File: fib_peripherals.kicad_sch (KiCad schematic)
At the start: 2 parts, among them J704 Conn_02x20_Odd_Even, J801 Conn_02x20_Odd_Even

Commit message: started arranging the components on the board, added some more missing footprints. starting to think about the overall distribution of parts
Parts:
- removed J704, J801: Conn_02x20_Odd_Even, Connector_PinHeader_2.54mm:PinHeader_2x20_P2.54mm_Vertical, symbol Connector_Generic:Conn_02x20_Odd_Even
- added J1, J2: Raspi_Header, Fibel2:Raspberry_Bottom_Entry, symbol Fibel2:Raspi_Header
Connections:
- net D3V3: now also J1.1 (Pin_1), J1.17 (Pin_17)
- net GND: now also J1.14 (Pin_14), J1.20 (Pin_20), J1.25 (Pin_25), J1.30 (Pin_30), J1.34 (Pin_34), J1.39 (Pin_39), J1.6 (Pin_6), J1.9 (Pin_9), J2.14 (Pin_14), J2.20 (Pin_20), J2.25 (Pin_25), J2.30 (Pin_30), J2.34 (Pin_34), J2.39 (Pin_39), J2.6 (Pin_6), J2.9 (Pin_9)
- net I2C1_SCL: now also J1.5 (Pin_5)
- net I2C1_SDA: now also J1.3 (Pin_3)
- net I2S0_DIN: now also J1.38 (Pin_38)
- net I2S0_DOUT: now also J1.40 (Pin_40)
- net I2S0_FS: now also J1.35 (Pin_35)
- net I2S0_SCLK: now also J1.12 (Pin_12)
- net IT8951_HRDY0: now also J2.18 (Pin_18)
- net IT8951_RST0: now also J2.11 (Pin_11)
- net IT8951_SPI1_CS0: now also J2.24 (Pin_24)
- net IT8951_SPI1_MISO: now also J2.21 (Pin_21)
- net IT8951_SPI1_MOSI: now also J2.19 (Pin_19)
- net IT8951_SPI1_SCK: now also J2.23 (Pin_23)
- net RP_GPIO04: now also J1.7 (Pin_7)
- net RP_GPIO05: now also J1.29 (Pin_29)
- net RP_GPIO06: now also J1.31 (Pin_31)
- net RP_GPIO12: now also J1.32 (Pin_32)
- net RP_GPIO13: now also J1.33 (Pin_33)
- net RP_GPIO16: now also J1.36 (Pin_36)
- net RP_GPIO17: now also J1.11 (Pin_11)
- net RP_GPIO22: now also J1.15 (Pin_15)
- net RP_GPIO23: now also J1.16 (Pin_16)
- net RP_GPIO24: now also J1.18 (Pin_18)
- net RP_GPIO25: now also J1.22 (Pin_22)
- net RP_GPIO26: now also J1.37 (Pin_37)
- net RP_GPIO27: now also J1.13 (Pin_13)
- net RP_ID_SC: now also J1.28 (Pin_28)
- net RP_ID_SD: now also J1.27 (Pin_27)
- net SPI0_CS0: now also J1.24 (Pin_24)
- net SPI0_CS1: now also J1.26 (Pin_26)
- net SPI0_MISO: now also J1.21 (Pin_21)
- net SPI0_MOSI: now also J1.19 (Pin_19)
- net SPI0_SCK: now also J1.23 (Pin_23)
- net UART1_RXD: now also J1.10 (Pin_10)
- net UART1_TXD: now also J1.8 (Pin_8)
- net VDD_MOD: now also J1.2 (Pin_2), J1.4 (Pin_4), J2.2 (Pin_2), J2.4 (Pin_4)

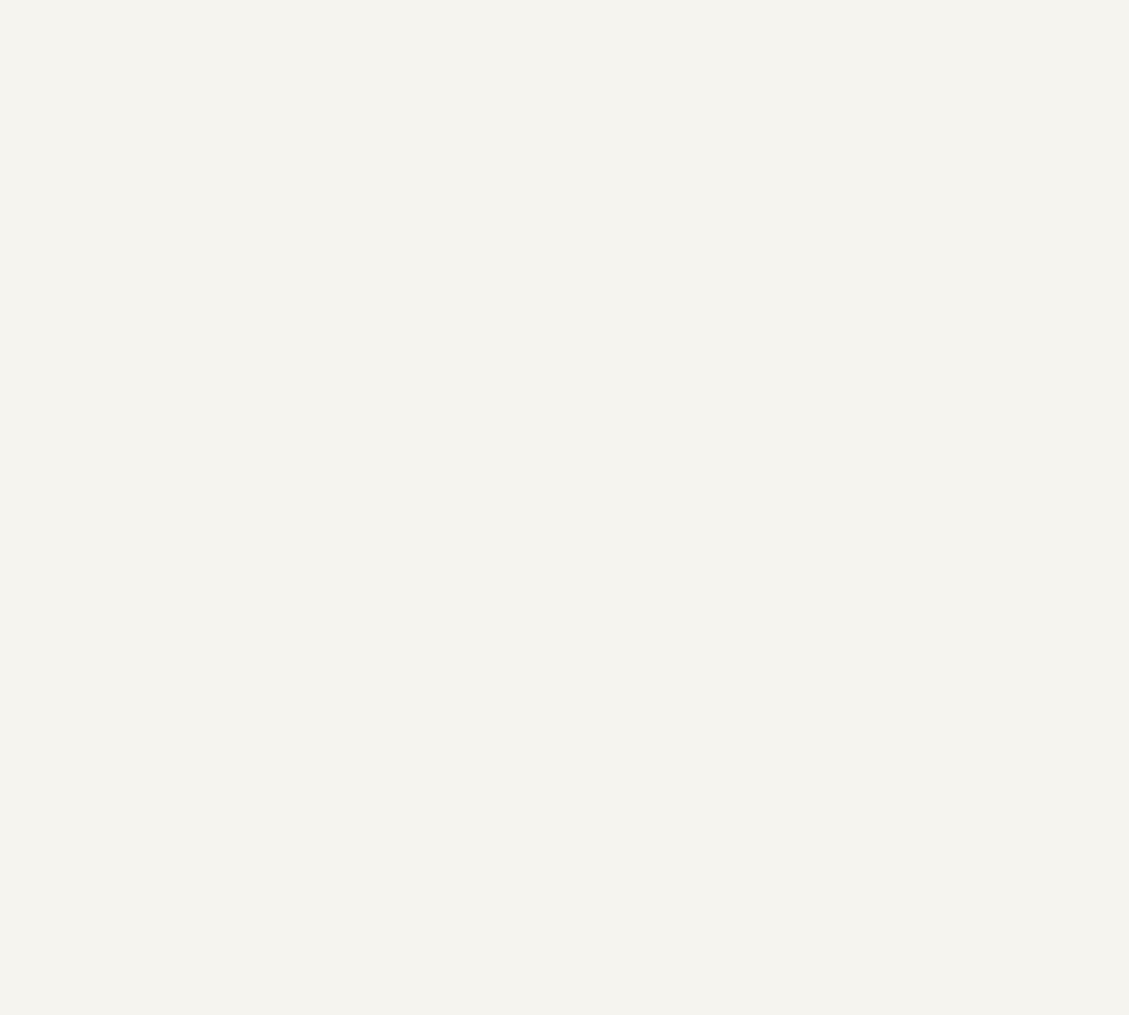
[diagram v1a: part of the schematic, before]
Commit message: replaced 1v8 buck with ldo, added startup circuit, added footprints for eink connectors
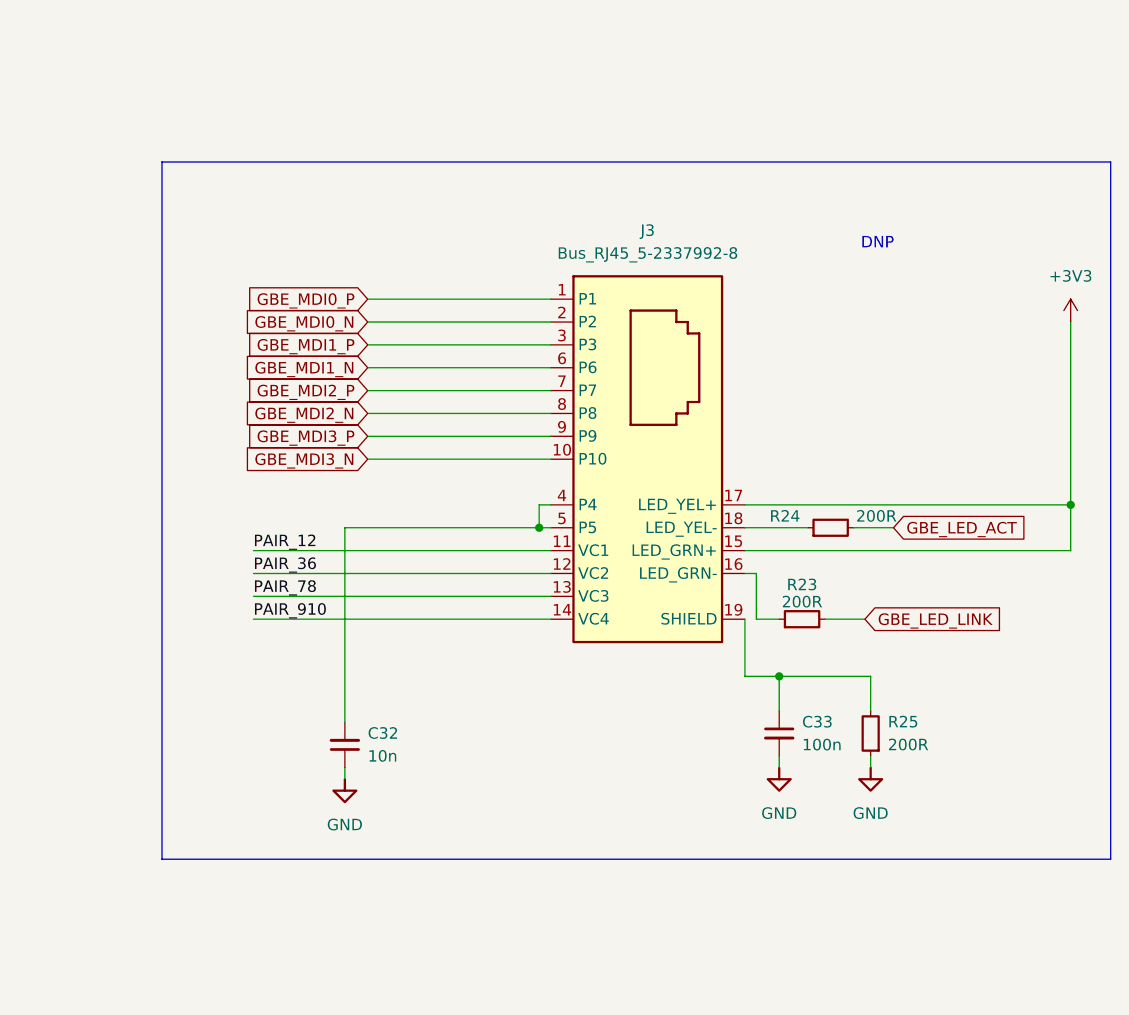
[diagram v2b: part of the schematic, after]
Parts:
- added C32: C_10n_0603, antmicro-footprints:C_0603_1608Metric, symbol antmicroCapacitors0603:C_10n_0603
- added C33: C_100n_0402, antmicro-footprints:C_0402_1005Metric, symbol antmicroCapacitors0402:C_100n_0402
- added J3: Bus_RJ45_5-2337992-8, antmicro-footprints:RJ45_X-2337992-8_Horizontal, symbol antmicroModularConnectorsJacksWithMagnetics:Bus_RJ45_5-2337992-8
- added R23, R24, R25: R_200R_0402, antmicro-footprints:R_0402_1005Metric, symbol antmicroResistors0402:R_200R_0402
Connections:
- net GND: now also C32.1, C33.2, R25.1
- new net: J3.18 (LED_YEL-), R24.1
- new net: C33.1, J3.19 (SHIELD), J3.20 (SHIELD), R25.2
- new net: C32.2, J3.4 (P4), J3.5 (P5)
- new net: J3.16 (LED_GRN-), R23.1
- new net +3V3: J3.15 (LED_GRN+), J3.17 (LED_YEL+)
- new net GBE_LED_ACT: R24.2
- new net GBE_LED_LINK: R23.2
- new net GBE_MDI0_N: J3.2 (P2)
- new net GBE_MDI0_P: J3.1 (P1)
- new net GBE_MDI1_N: J3.6 (P6)
- new net GBE_MDI1_P: J3.3 (P3)
- new net GBE_MDI2_N: J3.8 (P8)
- new net GBE_MDI2_P: J3.7 (P7)
- new net GBE_MDI3_N: J3.10 (P10)
- new net GBE_MDI3_P: J3.9 (P9)
- new net PAIR_12: J3.11 (VC1)
- new net PAIR_36: J3.12 (VC2)
- new net PAIR_78: J3.13 (VC3)
- new net PAIR_910: J3.14 (VC4)
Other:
- note added: "DNP"

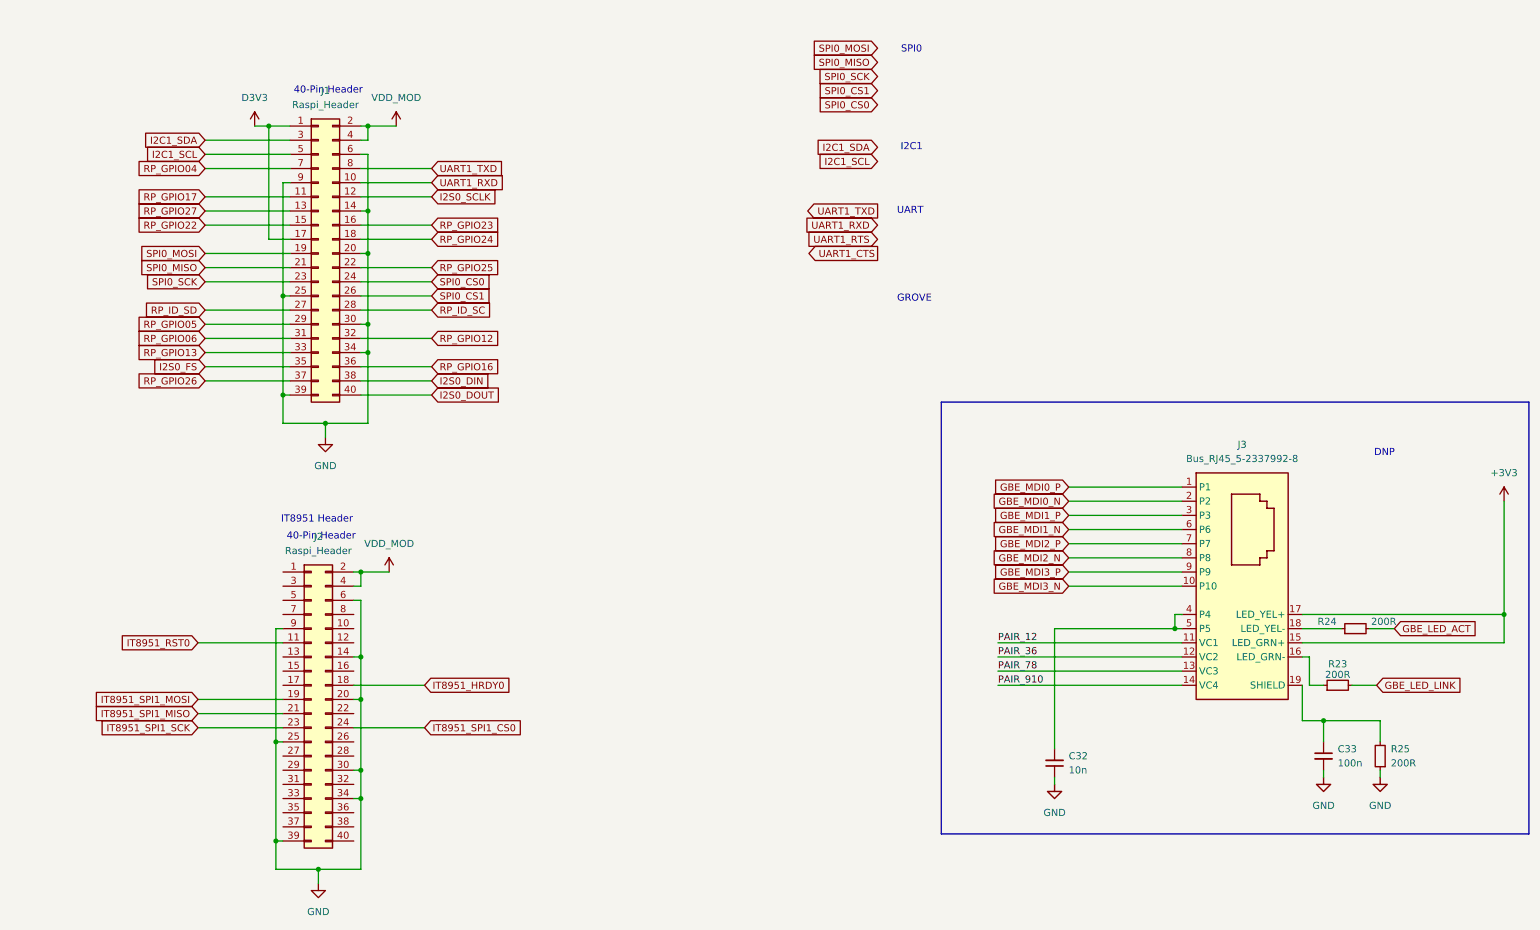
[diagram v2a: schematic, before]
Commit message: added all missing footprints, fixed library & footprint links, did layout out 99% of components, all that's left is rtc(?), peripherals, routing & lengthmatching and final sanity checks
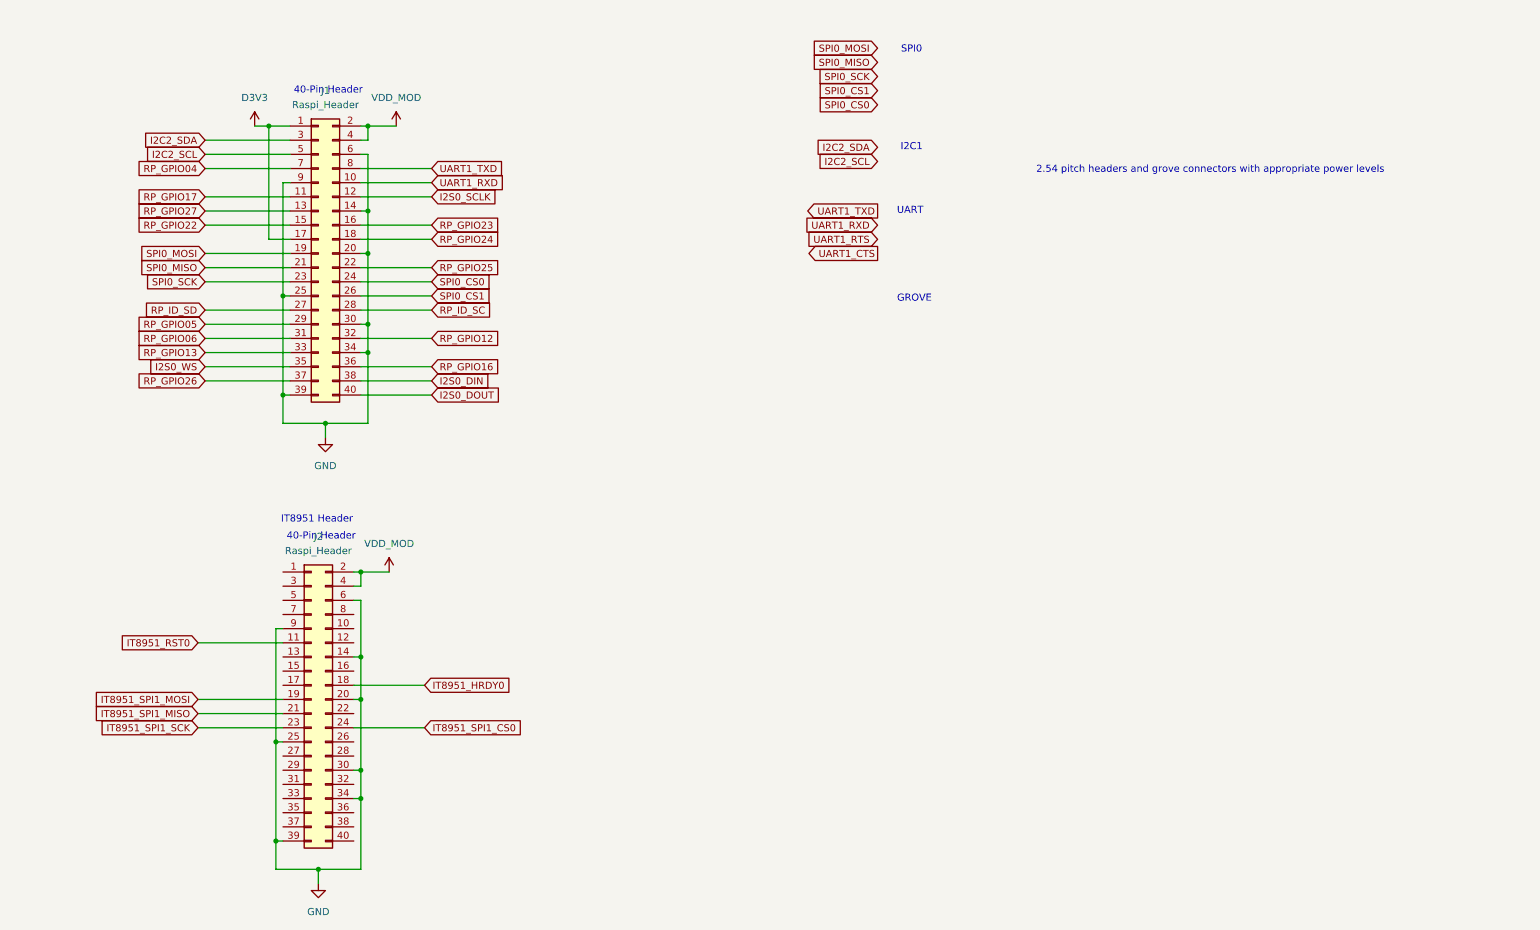
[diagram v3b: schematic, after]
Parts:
- removed C32: C_10n_0603, antmicro-footprints:C_0603_1608Metric, symbol antmicroCapacitors0603:C_10n_0603
- removed C33: C_100n_0402, antmicro-footprints:C_0402_1005Metric, symbol antmicroCapacitors0402:C_100n_0402
- removed J3: Bus_RJ45_5-2337992-8, antmicro-footprints:RJ45_X-2337992-8_Horizontal, symbol antmicroModularConnectorsJacksWithMagnetics:Bus_RJ45_5-2337992-8
- removed R23, R24, R25: R_200R_0402, antmicro-footprints:R_0402_1005Metric, symbol antmicroResistors0402:R_200R_0402
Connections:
- net I2C1_SCL renamed I2C2_SCL
- net I2C1_SDA renamed I2C2_SDA
- net I2S0_FS renamed I2S0_WS
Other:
- note added: "2.54 pitch headers and grove connectors with appropriate power levels"
- note removed: "DNP"

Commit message: did length tuning, routing of final submodules and most of power routing
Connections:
- net D3V3 renamed +3V3
- net VDD_MOD renamed +5V
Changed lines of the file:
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@@
+	)
+	(symbol
+		(lib_id "power:+3V3")
+		(at 54.61 39.37 0)
+		(unit 1)
+		(exclude_from_sim no)
+		(in_bom yes)
+		(on_board yes)
+		(dnp no)
+		(fields_autoplaced yes)
+		(property "Reference" "#PWR083"
+			(at 54.61 43.18 0)
+			(effects
+				(font
+					(size 1.27 1.27)
+				)
+				(hide yes)
+			)
+		)
+		(property "Value" "+3V3"
+			(at 54.61 34.29 0)
+			(effects
+				(font
+					(size 1.27 1.27)
+				)
+			)
+		)
+		(property "Footprint" ""
+			(at 54.61 39.37 0)
+			(effects
+				(font
+					(size 1.27 1.27)
+				)
+				(hide yes)
+			)
+		)
+		(property "Datasheet" ""
+			(at 54.61 39.37 0)
+			(effects
+				(font
+					(size 1.27 1.27)
+				)
+				(hide yes)
+			)
+		)
+		(property "Description" "Power symbol creates a global label with name \"+3V3\""
+			(at 54.61 39.37 0)
+			(effects
+				(font
+					(size 1.27 1.27)
+				)
+				(hide yes)
+			)
+		)
+		(pin "1"
+		)
+		(instances
+			(project "Fibel2"
+				(path "/862c21e2-7ec9-4f80-a33c-aad02ea9423e/a39c2c52-3412-48a6-9504-27933873c1ba"
+					(reference "#PWR083")
+					(unit 1)
+				)
+			)
+		)
 	)
 	(symbol
@@
 	)
 	(symbol
+		(lib_id "power:+5V")
+		(at 80.01 39.37 0)
+		(unit 1)
+		(exclude_from_sim no)
+		(in_bom yes)
+		(on_board yes)
+		(dnp no)
+		(fields_autoplaced yes)
+		(property "Reference" "#PWR082"
+			(at 80.01 43.18 0)
+			(effects
+				(font
+					(size 1.27 1.27)
+				)
+				(hide yes)
+			)
+		)
+		(property "Value" "+5V"
+			(at 80.01 34.29 0)
+			(effects
+				(font
+					(size 1.27 1.27)
+				)
+			)
+		)
+		(property "Footprint" ""
+			(at 80.01 39.37 0)
+			(effects
+				(font
+					(size 1.27 1.27)
+				)
+				(hide yes)
+			)
+		)
+		(property "Datasheet" ""
+			(at 80.01 39.37 0)
+			(effects
+				(font
+					(size 1.27 1.27)
+				)
+				(hide yes)
+			)
+		)
+		(property "Description" "Power symbol creates a global label with name \"+5V\""
+			(at 80.01 39.37 0)
+			(effects
+				(font
+					(size 1.27 1.27)
+				)
+				(hide yes)
+			)
+		)
+		(pin "1"
+		)
+		(instances
+			(project "Fibel2"
+				(path "/862c21e2-7ec9-4f80-a33c-aad02ea9423e/a39c2c52-3412-48a6-9504-27933873c1ba"
+					(reference "#PWR082")
+					(unit 1)
+				)
+			)
+		)
+	)
+	(symbol
 		(lib_id "Fibel2:Raspi_Header")
 		(at 66.04 62.23 0)
@@
 				(path "/862c21e2-7ec9-4f80-a33c-aad02ea9423e/a39c2c52-3412-48a6-9504-27933873c1ba"
 					(reference "J1")
-					(unit 1)
-				)
-			)
-		)
-	)
-	(symbol
-		(lib_id "power:+5V")
-		(at 78.74 119.38 0)
-		(unit 1)
-		(exclude_from_sim no)
-		(in_bom yes)
-		(on_board yes)
-		(dnp no)
-		(fields_autoplaced yes)
-		(property "Reference" "#PWR0713"
-			(at 78.74 123.19 0)
-			(effects
-				(font
-					(size 1.27 1.27)
-				)
-				(hide yes)
-			)
-		)
-		(property "Value" "VDD_MOD"
-			(at 78.74 114.3 0)
-			(effects
-				(font
-					(size 1.27 1.27)
-				)
-			)
-		)
-		(property "Footprint" ""
-			(at 78.74 119.38 0)
-			(effects
-				(font
-					(size 1.27 1.27)
-				)
-				(hide yes)
-			)
-		)
-		(property "Datasheet" ""
-			(at 78.74 119.38 0)
-			(effects
-				(font
-					(size 1.27 1.27)
-				)
-				(hide yes)
-			)
-		)
-		(property "Description" "Power symbol creates a global label with name \"+5V\""
-			(at 78.74 119.38 0)
-			(effects
-				(font
-					(size 1.27 1.27)
-				)
-				(hide yes)
-			)
-		)
-		(pin "1"
-		)
-		(instances
-			(project "Fibel2"
-				(path "/862c21e2-7ec9-4f80-a33c-aad02ea9423e/a39c2c52-3412-48a6-9504-27933873c1ba"
-					(reference "#PWR0713")
 					(unit 1)
 				)
@@
 	)
 	(symbol
-		(lib_id "power:+3V3")
-		(at 54.61 39.37 0)
+		(lib_id "power:+5V")
+		(at 78.74 119.38 0)
 		(unit 1)
 		(exclude_from_sim no)
@@
 		(dnp no)
 		(fields_autoplaced yes)
-		(property "Reference" "#PWR0801"
-			(at 54.61 43.18 0)
-			(effects
-				(font
-					(size 1.27 1.27)
-				)
-				(hide yes)
-			)
-		)
-		(property "Value" "D3V3"
-			(at 54.61 34.29 0)
+		(property "Reference" "#PWR081"
+			(at 78.74 123.19 0)
+			(effects
+				(font
+					(size 1.27 1.27)
+				)
+				(hide yes)
+			)
+		)
+		(property "Value" "+5V"
+			(at 78.74 114.3 0)
 			(effects
 				(font
@@
 		)
 		(property "Footprint" ""
-			(at 54.61 39.37 0)
+			(at 78.74 119.38 0)
 			(effects
 				(font
@@
 		)
 		(property "Datasheet" ""
-			(at 54.61 39.37 0)
-			(effects
-				(font
-					(size 1.27 1.27)
-				)
-				(hide yes)
-			)
-		)
-		(property "Description" "Power symbol creates a global label with name \"+3V3\""
-			(at 54.61 39.37 0)
+			(at 78.74 119.38 0)
+			(effects
+				(font
+					(size 1.27 1.27)
+				)
+				(hide yes)
+			)
+		)
+		(property "Description" "Power symbol creates a global label with name \"+5V\""
+			(at 78.74 119.38 0)
 			(effects
 				(font
@@
 			(project "Fibel2"
 				(path "/862c21e2-7ec9-4f80-a33c-aad02ea9423e/a39c2c52-3412-48a6-9504-27933873c1ba"
-					(reference "#PWR0801")
+					(reference "#PWR081")
 					(unit 1)
 				)
@@
 					(unit 1)
 				)
-			)
-		)
-	)
-	(symbol
-		(lib_id "power:+5V")
-		(at 80.01 39.37 0)
-		(unit 1)
-		(exclude_from_sim no)
-		(in_bom yes)
-		(on_board yes)
-		(dnp no)
-		(fields_autoplaced yes)
-		(property "Reference" "#PWR0803"
-			(at 80.01 43.18 0)
-			(effects
-				(font
-					(size 1.27 1.27)
-				)
-				(hide yes)
-			)
-		)
-		(property "Value" "VDD_MOD"
-			(at 80.01 34.29 0)
-			(effects
-				(font
-					(size 1.27 1.27)
-				)
-			)
-		)
-		(property "Footprint" ""
-			(at 80.01 39.37 0)
-			(effects
-				(font
-					(size 1.27 1.27)
-				)
-				(hide yes)
-			)
-		)
-		(property "Datasheet" ""
-			(at 80.01 39.37 0)
-			(effects
-				(font
-					(size 1.27 1.27)
-				)
-				(hide yes)
-			)
-		)
-		(property "Description" "Power symbol creates a global label with name \"+5V\""
-			(at 80.01 39.37 0)
-			(effects
-				(font
-					(size 1.27 1.27)
-				)
-				(hide yes)
-			)
-		)
-		(pin "1"
-		)
-		(instances
-			(project "Fibel2"
-				(path "/862c21e2-7ec9-4f80-a33c-aad02ea9423e/a39c2c52-3412-48a6-9504-27933873c1ba"
-					(reference "#PWR0803")
-					(unit 1)
-				)
